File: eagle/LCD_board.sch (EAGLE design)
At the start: 5 parts, among them CN1 1X4-CLEANBIG

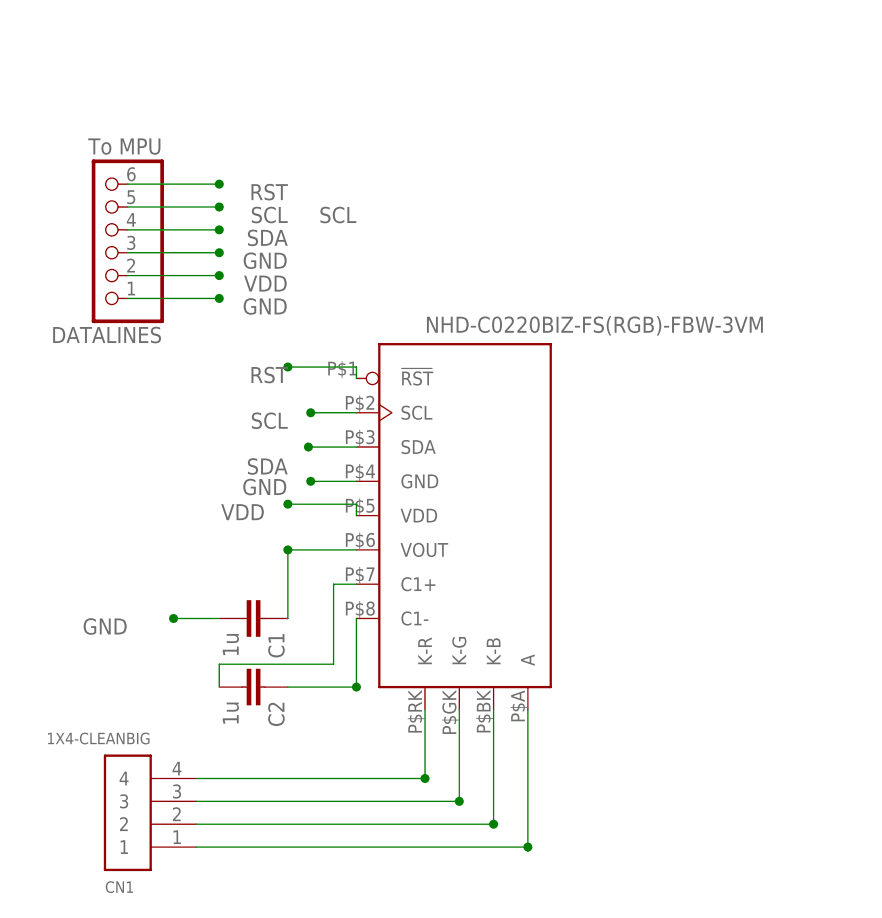
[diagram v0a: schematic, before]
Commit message: LCD board with pull up resistor
This should give us a working screen with thru hole components just to
check dimensions and use for debug. Next change resistor and capacitor
for surface mount and determine if RGB resistors will be on this or the
main board.
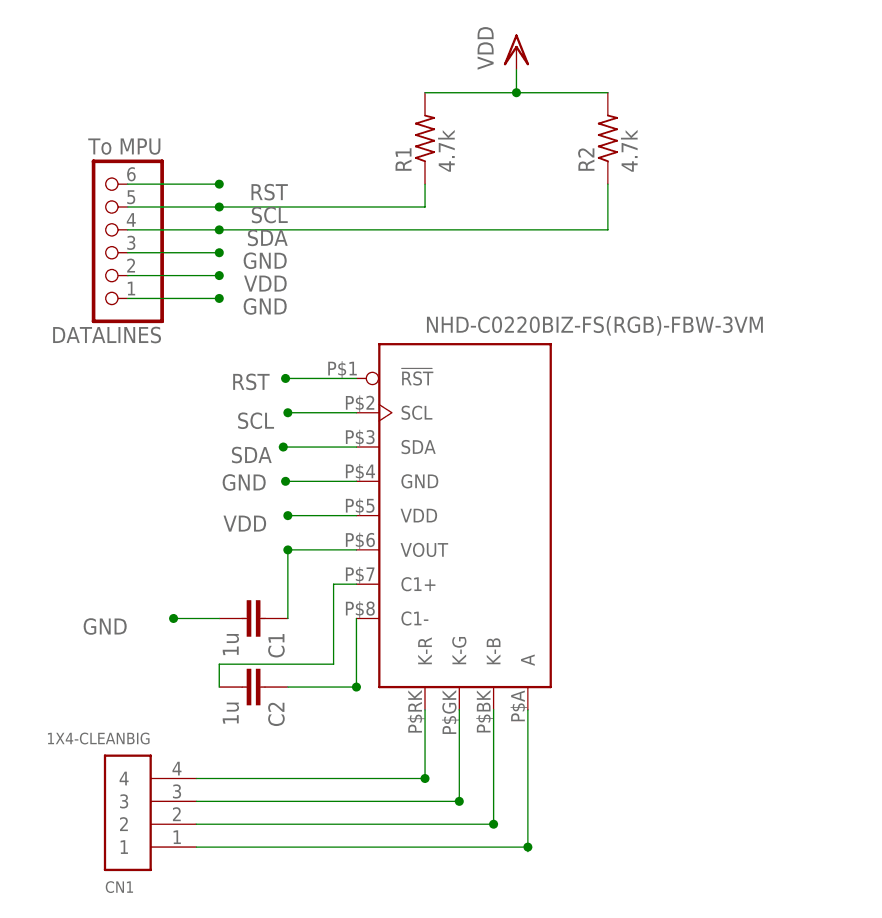
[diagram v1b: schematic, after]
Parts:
- added R1, R2: 4.7k, LockBox:R-US_0204/5
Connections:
- net SCL: now also R1.1
- net SDA: now also R2.1
- net VDD: now also R1.2, R2.2
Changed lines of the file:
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@@
 <part name="C2" library="capacitor-wima" deviceset="C" device="15/8" value="1u"/>
 <part name="CN1" library="adafruit" deviceset="1X4" device="-CLEANBIG"/>
+<part name="R1" library="LockBox" deviceset="R-US_" device="0204/5" value="4.7k"/>
+<part name="R2" library="LockBox" deviceset="R-US_" device="0204/5" value="4.7k"/>
+<part name="VDD1" library="supply1" deviceset="VDD" device=""/>
 </parts>
 <sheets>
@@
 <instance part="C2" gate="G$1" x="81.28" y="12.7" rot="R270"/>
 <instance part="CN1" gate="G$1" x="68.58" y="-2.54" rot="R180"/>
+<instance part="R1" gate="G$1" x="99.06" y="73.66" rot="R90"/>
+<instance part="R2" gate="G$1" x="119.38" y="73.66" rot="R90"/>
+<instance part="VDD1" gate="G$1" x="109.22" y="83.82"/>
 </instances>
 <busses>
@@
 <net name="RST" class="0">
 <segment>
-<junction x="83.82" y="48.26"/>
-<label x="83.82" y="48.26" size="1.778" layer="95" rot="R180"/>
+<junction x="83.566" y="46.99"/>
+<label x="81.788" y="47.498" size="1.778" layer="95" rot="R180"/>
 <pinref part="U$1" gate="G$1" pin="!RST"/>
-<wire x1="91.44" y1="46.99" x2="91.44" y2="48.26" width="0.1524" layer="91"/>
-<wire x1="91.44" y1="48.26" x2="83.82" y2="48.26" width="0.1524" layer="91"/>
+<wire x1="91.44" y1="46.99" x2="83.566" y2="46.99" width="0.1524" layer="91"/>
 </segment>
 <segment>
@@
 <wire x1="66.04" y1="66.04" x2="76.2" y2="66.04" width="0.1524" layer="91"/>
 <junction x="76.2" y="66.04"/>
-<label x="91.44" y="66.04" size="1.778" layer="95" rot="R180"/>
 <label x="83.82" y="66.04" size="1.778" layer="95" rot="R180"/>
+<pinref part="R1" gate="G$1" pin="1"/>
+<wire x1="76.2" y1="66.04" x2="99.06" y2="66.04" width="0.1524" layer="91"/>
+<wire x1="99.06" y1="66.04" x2="99.06" y2="68.58" width="0.1524" layer="91"/>
 </segment>
 <segment>
 <pinref part="U$1" gate="G$1" pin="SCL"/>
-<wire x1="91.44" y1="43.18" x2="86.36" y2="43.18" width="0.1524" layer="91"/>
-<junction x="86.36" y="43.18"/>
-<label x="83.82" y="43.18" size="1.778" layer="95" rot="R180"/>
+<wire x1="91.44" y1="43.18" x2="83.82" y2="43.18" width="0.1524" layer="91"/>
+<junction x="83.82" y="43.18"/>
+<label x="82.296" y="43.18" size="1.778" layer="95" rot="R180"/>
 </segment>
 </net>
@@
 <junction x="76.2" y="63.5"/>
 <label x="83.82" y="63.5" size="1.778" layer="95" rot="R180"/>
+<pinref part="R2" gate="G$1" pin="1"/>
+<wire x1="119.38" y1="68.58" x2="119.38" y2="63.5" width="0.1524" layer="91"/>
+<wire x1="119.38" y1="63.5" x2="76.2" y2="63.5" width="0.1524" layer="91"/>
 </segment>
 <segment>
 <pinref part="U$1" gate="G$1" pin="SDA"/>
-<wire x1="91.44" y1="39.37" x2="86.106" y2="39.37" width="0.1524" layer="91"/>
-<junction x="86.106" y="39.37"/>
-<label x="83.82" y="38.1" size="1.778" layer="95" rot="R180"/>
+<wire x1="91.44" y1="39.37" x2="83.312" y2="39.37" width="0.1524" layer="91"/>
+<junction x="83.312" y="39.37"/>
+<label x="82.042" y="39.37" size="1.778" layer="95" rot="R180"/>
 </segment>
 </net>
@@
 </segment>
 <segment>
-<wire x1="91.44" y1="31.75" x2="91.44" y2="33.02" width="0.1524" layer="91"/>
-<wire x1="91.44" y1="33.02" x2="83.82" y2="33.02" width="0.1524" layer="91"/>
-<junction x="83.82" y="33.02"/>
-<label x="81.28" y="33.02" size="1.778" layer="95" rot="R180"/>
+<wire x1="91.44" y1="31.75" x2="83.82" y2="31.75" width="0.1524" layer="91"/>
+<junction x="83.82" y="31.75"/>
+<label x="81.534" y="31.75" size="1.778" layer="95" rot="R180"/>
 <pinref part="U$1" gate="G$1" pin="VDD"/>
+</segment>
+<segment>
+<pinref part="R1" gate="G$1" pin="2"/>
+<pinref part="R2" gate="G$1" pin="2"/>
+<wire x1="99.06" y1="78.74" x2="109.22" y2="78.74" width="0.1524" layer="91"/>
+<wire x1="119.38" y1="78.74" x2="109.22" y2="78.74" width="0.1524" layer="91"/>
+<wire x1="109.22" y1="78.74" x2="109.22" y2="81.28" width="0.1524" layer="91"/>
+<junction x="109.22" y="78.74"/>
+<pinref part="VDD1" gate="G$1" pin="VDD"/>
 </segment>
 </net>
@@
 <segment>
 <pinref part="U$1" gate="G$1" pin="GND"/>
-<wire x1="91.44" y1="35.56" x2="86.36" y2="35.56" width="0.1524" layer="91"/>
-<junction x="86.36" y="35.56"/>
-<label x="78.74" y="34.036" size="1.778" layer="95"/>
+<wire x1="91.44" y1="35.56" x2="83.566" y2="35.56" width="0.1524" layer="91"/>
+<junction x="83.566" y="35.56"/>
+<label x="76.454" y="34.544" size="1.778" layer="95"/>
 </segment>
 <segment>
